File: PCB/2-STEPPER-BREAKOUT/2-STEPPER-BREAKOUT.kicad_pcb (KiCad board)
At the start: 2 copper layers, 15.2 x 50.3 mm, 3 parts, among them J1 Conn_01x04_Female, J2 Conn_01x04_Female, J3 Conn_01x08

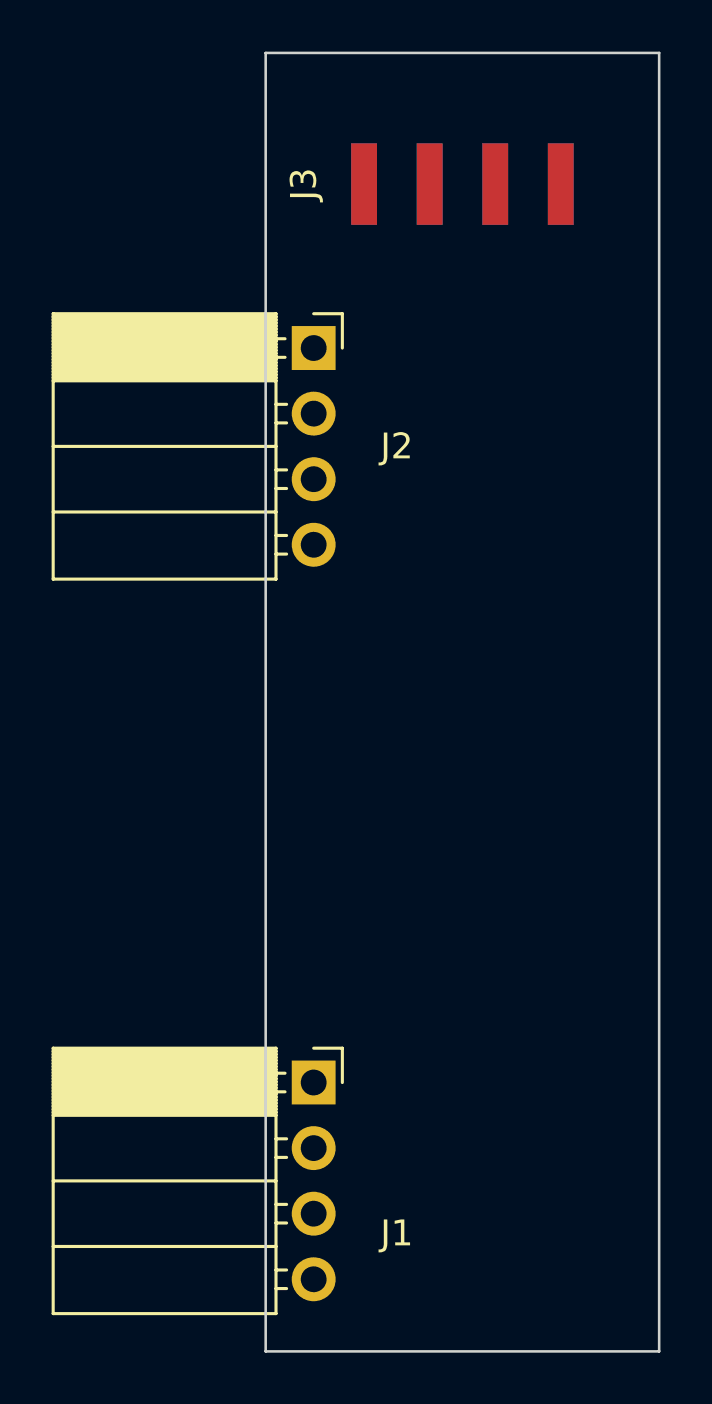
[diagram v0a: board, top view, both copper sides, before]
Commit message: Finish 2-motor breakout, submit order for 2 & 64
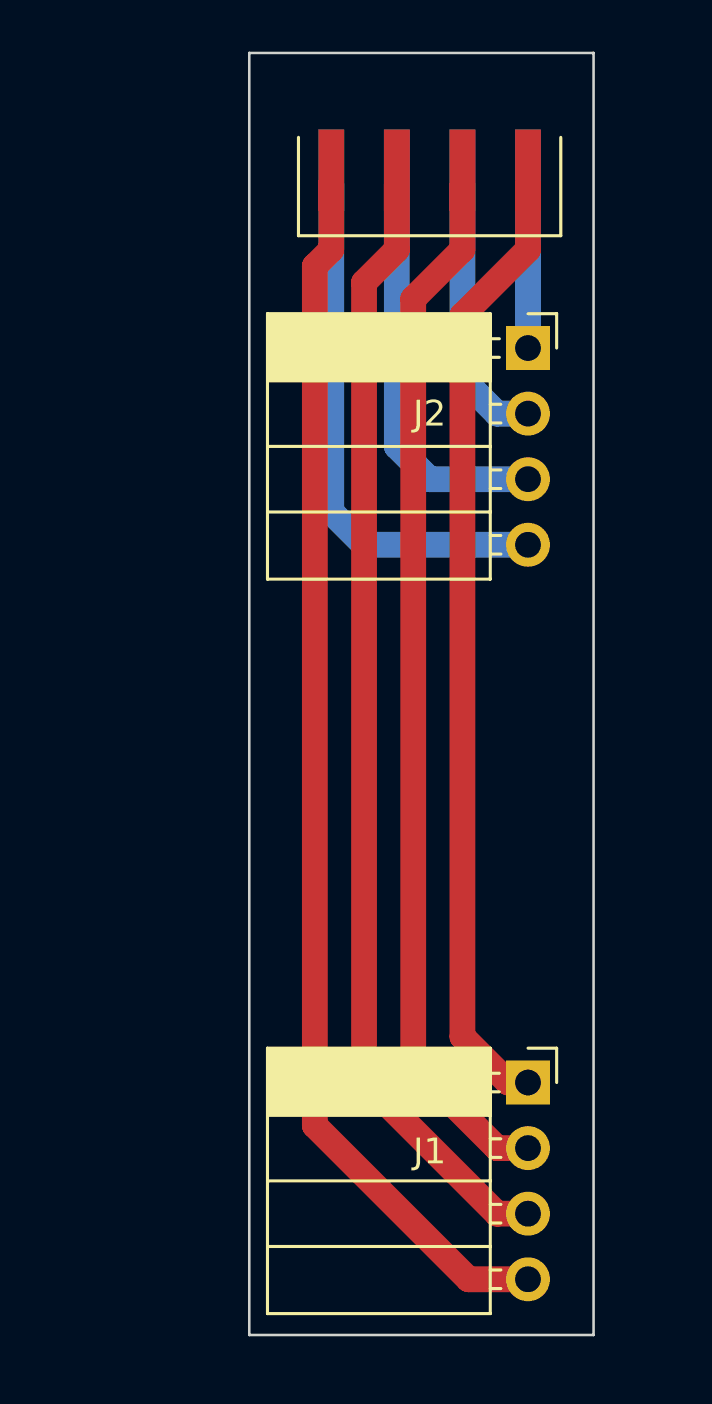
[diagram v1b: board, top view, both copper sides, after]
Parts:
- J3: moved to F.Cu
- moved J1 8.30 mm to (188.0, 78.0)
- moved J2 8.30 mm to (188.0, 49.5)
- moved J3 1.38 mm to (184.2, 40.1)
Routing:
- net Net-(J1-Pad4): track 0.00 -> 47.4 mm
- net Net-(J1-Pad3): track 0.00 -> 43.7 mm
- net Net-(J1-Pad2): track 0.00 -> 40.7 mm
- net Net-(J1-Pad1): track 0.00 -> 37.3 mm
- net Net-(J2-Pad4): track 0.00 -> 20.8 mm
- net Net-(J2-Pad3): track 0.00 -> 15.8 mm
- net Net-(J2-Pad2): track 0.00 -> 10.6 mm
- net Net-(J2-Pad1): track 0.00 -> 6.35 mm
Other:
- board size 15.2 x 50.3 mm -> 13.3 x 49.7 mm
